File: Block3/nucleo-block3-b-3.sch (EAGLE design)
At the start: 91 parts, among them IC1 TL331, J4 MODJACK6P6C-MJ3245-66-0CONN_M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, J5 MODJACK6P6C-MJ3245-66-0CONN_M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, Q1 NPN-23, Q2 BSS123, Q3 BSS84, U1 TC4428, U2 TC4428, U3 TC4428

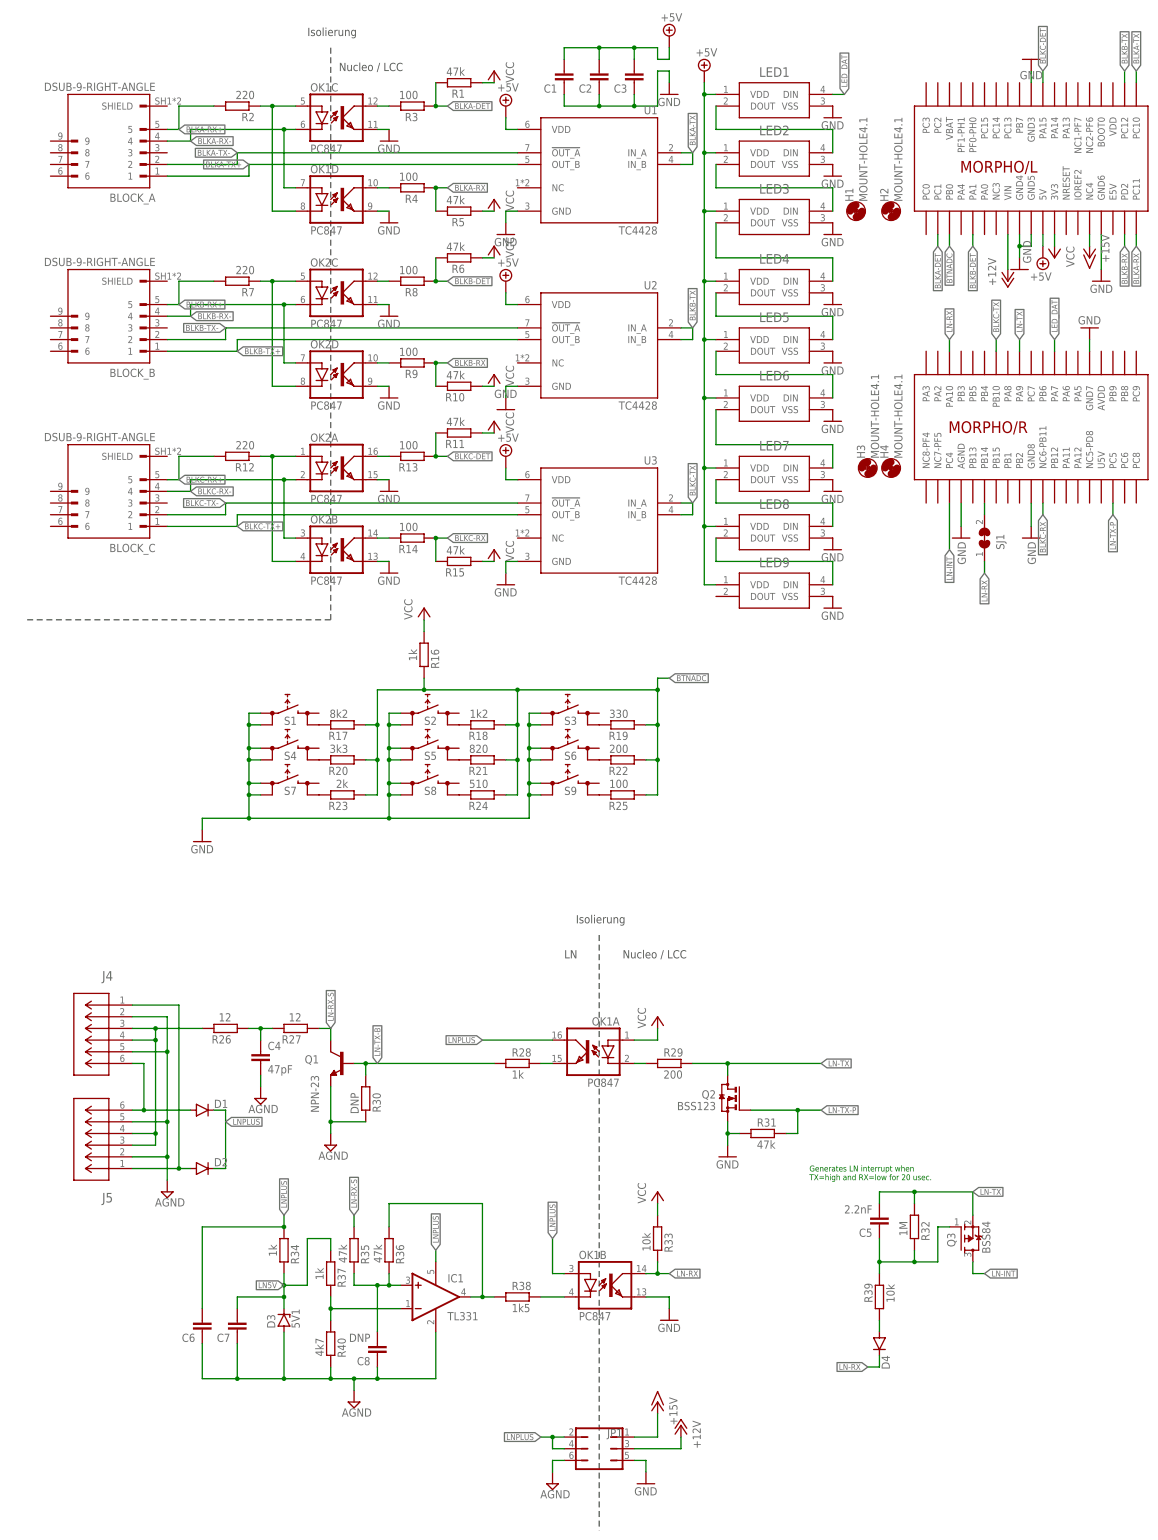
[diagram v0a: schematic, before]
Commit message: - adds a small TH pin "alignment hole" to the lib - fixes the DB-9 connector's pin order - updates the loconet-block3 board for rev B.
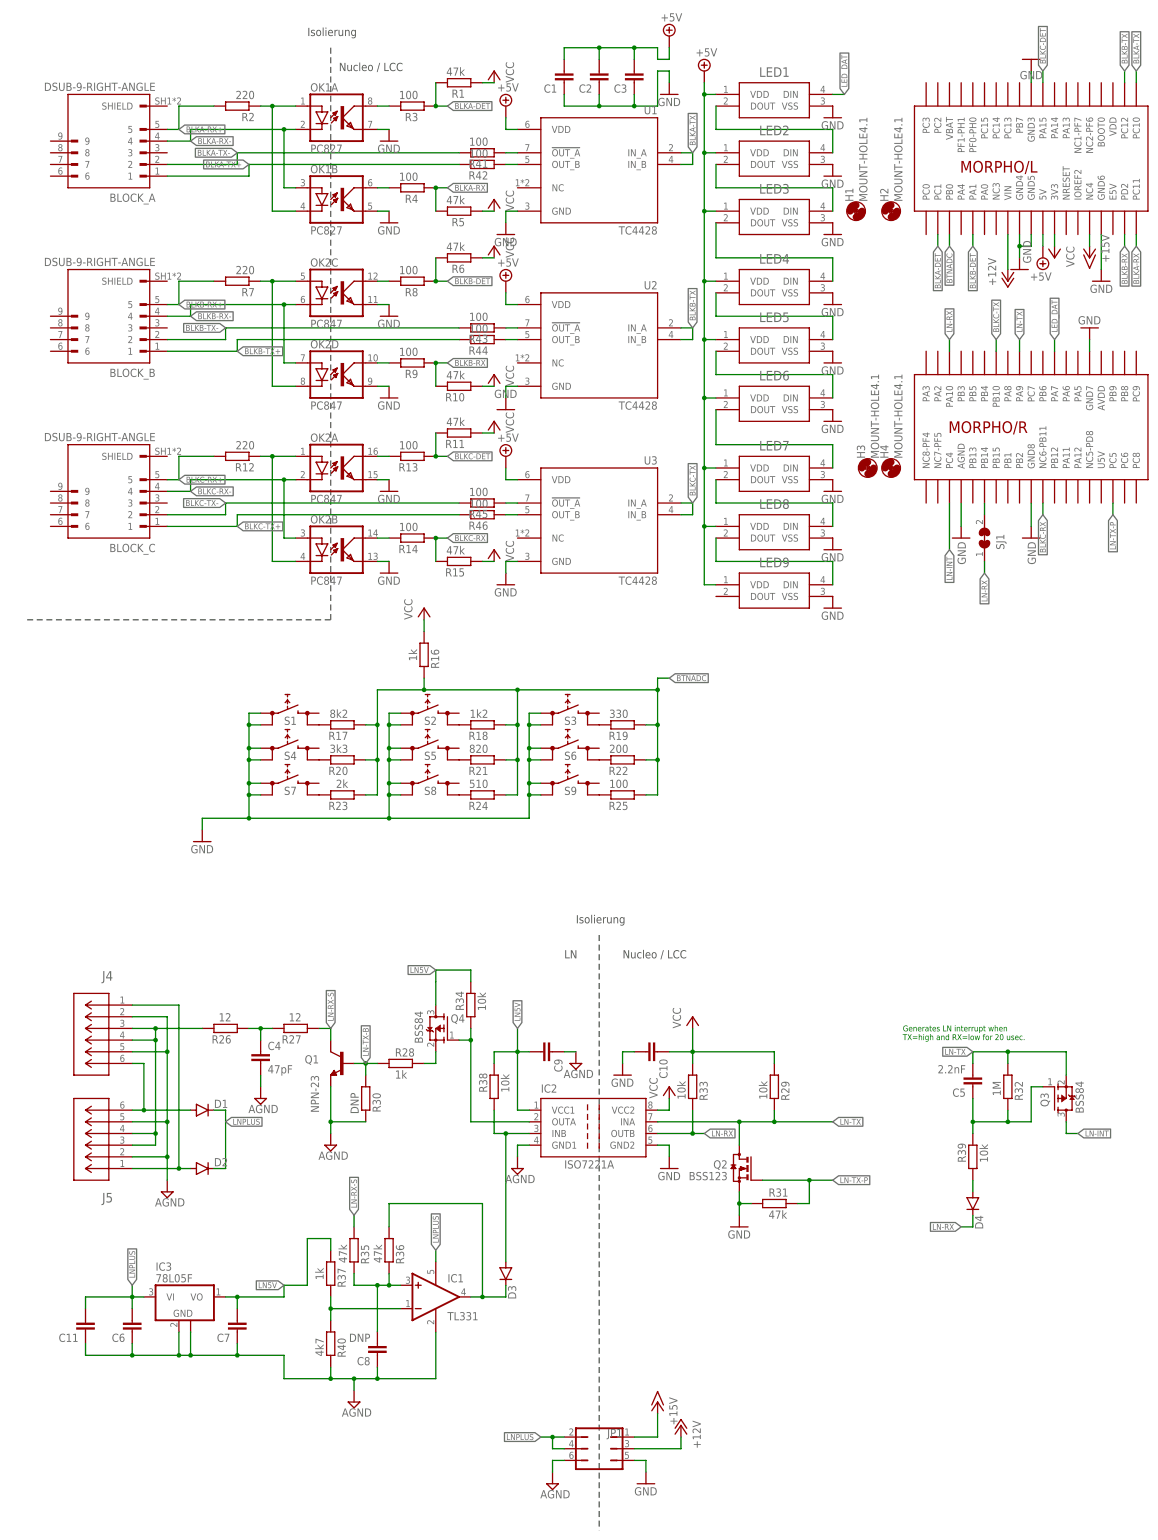
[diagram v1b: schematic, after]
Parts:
- added C10, C9: (no value), rcl:C-EUC0603
- added C11: (no value), rcl:C-EUC0603K
- added IC2: ISO7221A, texas:ISO7221A
- added IC3: 78L05F, linear:78L05F
- added Q4: BSS84, eagleparts:BSS84
- added R41, R42, R43, R44, R45, R46: 100, rcl:R-EU_R0805
- D3: value 5V1 -> (none); device diode:ZENER-DIODESOD80C -> diode:DIODE-MINIMELF
- OK1: value PC847 -> PC827; device optocoupler:PC847 -> optocoupler:PC827
- R29: value 200 -> 10k
- R34: value 1k -> 10k
- R38: value 1k5 -> 10k
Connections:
- new net N$20: D3.A, IC2.INB, R38.1
- new net N$24: R41.1, U1.!OUT_A
- new net N$25: R42.1, U1.OUT_B
- new net N$37: R43.1, U2.!OUT_A
- new net N$40: R46.1, U3.OUT_B
- new net N$8: IC2.OUTA, Q4.G, R34.1
- net AGND: now also C11.1, C9.1, IC2.GND1, IC3.GND, IC3.GND@1; no longer D3.A
- net BLKA-RX-: now also OK1A.C, OK1B.A; no longer OK1C.C, OK1D.A
- net BLKA-TX+: now also R42.2; no longer U1.OUT_B
- net BLKA-TX-: now also R41.2; no longer U1.!OUT_A
- net BLKB-TX+: now also R44.2; no longer U2.OUT_B
- net BLKB-TX-: now also R43.2; no longer U2.!OUT_A
- net BLKC-TX+: now also R46.2; no longer U3.OUT_B
- net BLKC-TX-: now also R45.2; no longer U3.!OUT_A
- net GND: now also C10.2, IC2.GND2, OK1A.EMIT; no longer OK1C.EMIT, OK1D.EMIT
- net LN-RX: now also IC2.OUTB; no longer OK1B.COL
- net LN-TX: now also IC2.INA
- net LN5V: now also C9.2, IC2.VCC1, IC3.VO, Q4.D, R38.2; no longer D3.C
- net LNPLUS: now also C11.2, IC3.VI; no longer OK1A.COL, OK1B.A, R34.1
- net N$11: now also Q4.S; no longer OK1A.EMIT
- net N$31: now also OK1A.A, OK1B.C; no longer OK1C.A, OK1D.C
- net N$36: now also D3.C; no longer R38.1
- net N$38: now also R44.1, U2.OUT_B; no longer OK1A.C, R29.1
- net N$39: now also R45.1, U3.!OUT_A; no longer OK1B.C, R38.2
- net N$41: now also OK1A.COL; no longer OK1C.COL
- net N$42: now also OK1B.COL; no longer OK1D.COL
- net VCC: now also C10.1, IC2.VCC2, R29.1; no longer OK1A.A
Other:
- moved on the sheet: C5, C6, D4, OK1A, OK1B, Q2, Q3, R28, R29, R31, R32, R33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
